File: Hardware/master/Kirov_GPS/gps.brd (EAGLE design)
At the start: 100 x 80 mm, 7 parts

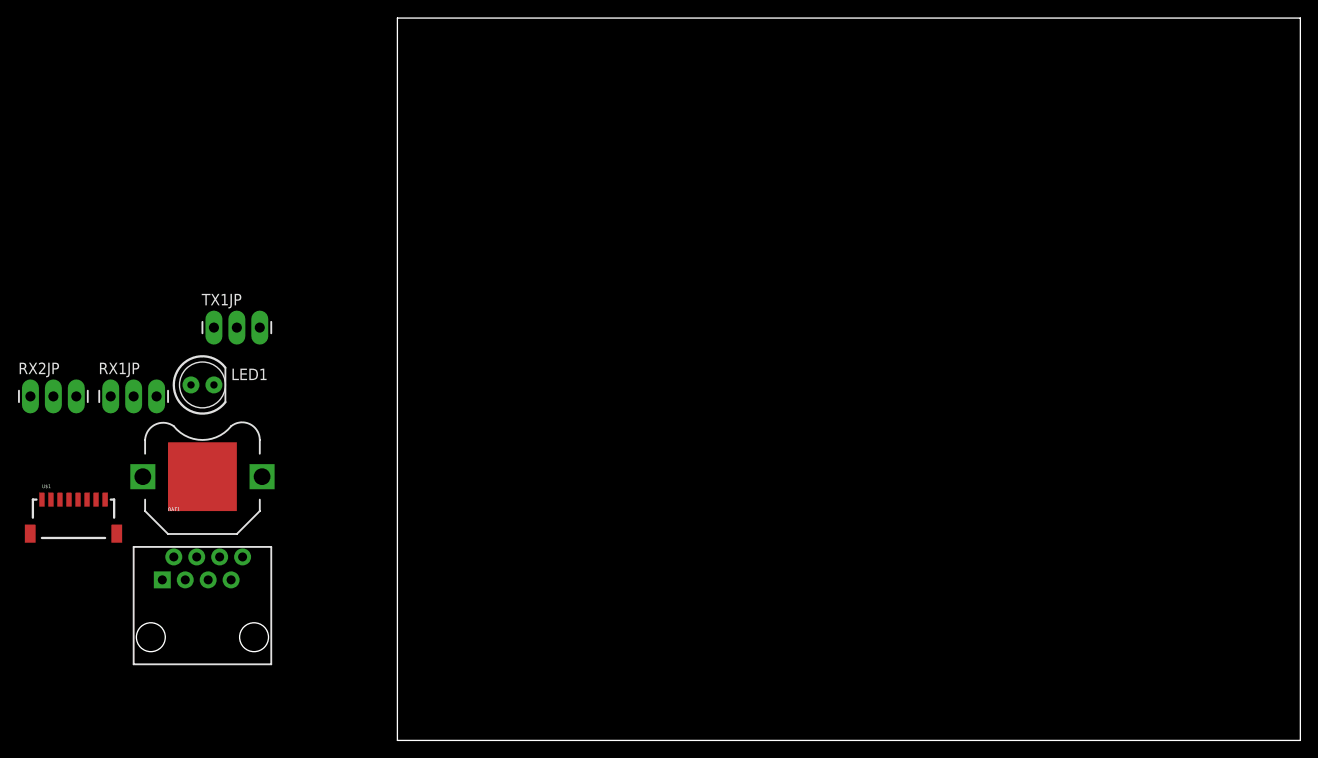
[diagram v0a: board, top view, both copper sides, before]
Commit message: added board layout and cap to schematic
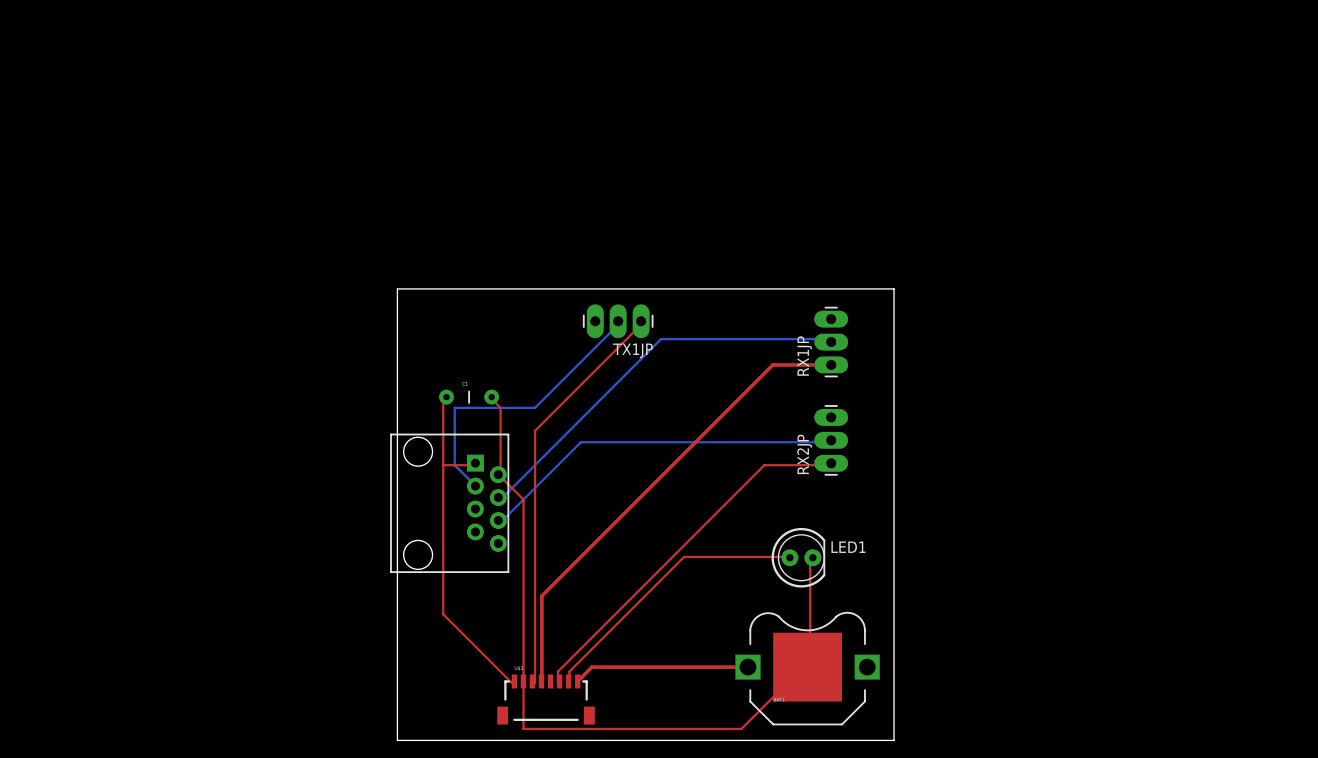
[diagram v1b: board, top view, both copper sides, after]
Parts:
- added C1: 100 uf, SparkFun-Passives:CAP-PTH-5MM
- moved RX2JP 89.0 mm to (48.0, 30.7), turned to 90 degrees
- moved RX1JP 79.9 mm to (48.0, 41.6), turned to 90 degrees
- moved BAT1 70.3 mm to (45.4, 8.12)
- moved LED1 69.0 mm to (44.7, 20.2)
- moved U$1 56.1 mm to (13.0, 6.53)
- moved TX1JP 47.3 mm to (27.0, 46.4), turned to 180 degrees
- moved GPS2ZYNQ 28.1 mm to (2.29, 26.3), turned to 270 degrees
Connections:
- net GND: now also C1.2
- net VCC: now also C1.1
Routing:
- net GND: track 0.00 -> 86.0 mm
- net RX1: track 0.00 -> 52.1 mm
- net TX1: track 0.00 -> 45.2 mm
- net ZRX1: track 0.00 -> 44.4 mm
- net RX2: track 0.00 -> 41.3 mm
- net ZRX2: track 0.00 -> 40.6 mm
- net VCC: track 0.00 -> 39.7 mm
- net ZTX1: track 0.00 -> 32.5 mm
- net PPS: track 0.00 -> 31.2 mm
- net BATT: track 0.00 -> 19.5 mm
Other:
- board size 100 x 80 mm -> 55 x 50 mm
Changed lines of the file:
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@@
 <setting verticaltext="up"/>
 </settings>
-<grid distance="0.05" unitdist="inch" unit="inch" style="lines" multiple="1" display="no" altdistance="0.025" altunitdist="inch" altunit="inch"/>
+<grid distance="1" unitdist="mm" unit="mm" style="lines" multiple="1" display="no" altdistance="0.1" altunitdist="mm" altunit="mm"/>
 <layers>
 <layer number="1" name="Top" color="4" fill="1" visible="yes" active="yes"/>
@@
 <board>
 <plain>
-<wire x1="0" y1="0" x2="100" y2="0" width="0" layer="20"/>
-<wire x1="100" y1="0" x2="100" y2="80" width="0" layer="20"/>
-<wire x1="100" y1="80" x2="0" y2="80" width="0" layer="20"/>
-<wire x1="0" y1="80" x2="0" y2="0" width="0" layer="20"/>
+<wire x1="0" y1="0" x2="55" y2="0" width="0" layer="20"/>
+<wire x1="55" y1="0" x2="55" y2="50" width="0" layer="20"/>
+<wire x1="55" y1="50" x2="0" y2="50" width="0" layer="20"/>
+<wire x1="0" y1="50" x2="0" y2="0" width="0" layer="20"/>
 </plain>
 <attributes>
@@
 </autorouter>
 <elements>
-<element name="U$1" library="SparkFun-Connectors" package="EB-85A" value="EB-85ASMD" x="-39.37" y="26.67"/>
-<element name="GPS2ZYNQ" library="SparkFun-Connectors" package="RJ45-8" value="RJ45-8PTH" x="-21.59" y="11.43"/>
-<element name="LED1" library="SparkFun-LED" package="LED5MM" value="" x="-21.59" y="39.37"/>
-<element name="BAT1" library="SparkFun-Electromechanical" package="BATTCON_12MM_PTH" value="" x="-21.59" y="29.21"/>
-<element name="TX1JP" library="SparkFun-Connectors" package="1X03_LONGPADS" value="" x="-20.32" y="45.72"/>
-<element name="RX1JP" library="SparkFun-Connectors" package="1X03_LONGPADS" value="" x="-31.75" y="38.1"/>
-<element name="RX2JP" library="SparkFun-Connectors" package="1X03_LONGPADS" value="" x="-40.64" y="38.1"/>
+<element name="U$1" library="SparkFun-Connectors" package="EB-85A" value="EB-85ASMD" x="12.96" y="6.53"/>
+<element name="GPS2ZYNQ" library="SparkFun-Connectors" package="RJ45-8" value="RJ45-8PTH" x="2.29" y="26.26" rot="R270"/>
+<element name="LED1" library="SparkFun-LED" package="LED5MM" value="" x="44.74" y="20.23"/>
+<element name="BAT1" library="SparkFun-Electromechanical" package="BATTCON_12MM_PTH" value="" x="45.43" y="8.12"/>
+<element name="TX1JP" library="SparkFun-Connectors" package="1X03_LONGPADS" value="" x="26.99" y="46.42" rot="R180"/>
+<element name="RX1JP" library="SparkFun-Connectors" package="1X03_LONGPADS" value="" x="48.04" y="41.58" rot="R90"/>
+<element name="RX2JP" library="SparkFun-Connectors" package="1X03_LONGPADS" value="" x="48.04" y="30.69" rot="R90"/>
+<element name="C1" library="SparkFun-Passives" package="CAP-PTH-5MM" value="100 uf" x="7.94" y="38.02"/>
 </elements>
 <signals>
@@
 <contactref element="U$1" pad="1"/>
 <contactref element="GPS2ZYNQ" pad="1"/>
-<wire x1="-26.035" y1="17.78" x2="-39.37" y2="26.67" width="0" layer="19" extent="1-1"/>
+<contactref element="C1" pad="1"/>
+<wire x1="5.08" y1="13.97" x2="12.7" y2="6.35" width="0.254" layer="1"/>
+<wire x1="5.08" y1="38.1" x2="5.08" y2="30.48" width="0.254" layer="1"/>
+<wire x1="5.08" y1="30.48" x2="5.08" y2="13.97" width="0.254" layer="1"/>
+<wire x1="12.7" y1="6.35" x2="12.96" y2="6.53" width="0.254" layer="1"/>
+<wire x1="5.08" y1="38.1" x2="5.44" y2="38.02" width="0.254" layer="1"/>
+<wire x1="5.08" y1="30.48" x2="8.89" y2="30.48" width="0.254" layer="1"/>
+<wire x1="8.89" y1="30.48" x2="8.64" y2="30.705" width="0.254" layer="1"/>
 </signal>
 <signal name="GND">
@@
 <contactref element="LED1" pad="K"/>
 <contactref element="GPS2ZYNQ" pad="2"/>
-<wire x1="-21.59" y1="29.21" x2="-20.32" y2="39.37" width="0" layer="19" extent="1-1"/>
-<wire x1="-24.765" y1="20.32" x2="-21.59" y2="29.21" width="0" layer="19" extent="1-1"/>
-<wire x1="-38.37" y1="26.67" x2="-24.765" y2="20.32" width="0" layer="19" extent="1-1"/>
+<contactref element="C1" pad="2"/>
+<wire x1="45.72" y1="8.89" x2="45.72" y2="20.32" width="0.254" layer="1"/>
+<wire x1="45.72" y1="20.32" x2="46.01" y2="20.23" width="0.254" layer="1"/>
+<wire x1="45.72" y1="8.89" x2="45.43" y2="8.12" width="0.254" layer="1"/>
+<wire x1="13.97" y1="26.67" x2="13.97" y2="6.35" width="0.254" layer="1"/>
+<wire x1="11.43" y1="29.21" x2="13.97" y2="26.67" width="0.254" layer="1"/>
+<wire x1="11.43" y1="36.83" x2="10.16" y2="38.1" width="0.254" layer="1"/>
+<wire x1="11.43" y1="29.21" x2="11.43" y2="36.83" width="0.254" layer="1"/>
+<wire x1="10.16" y1="38.1" x2="10.44" y2="38.02" width="0.254" layer="1"/>
+<wire x1="11.43" y1="29.21" x2="11.18" y2="29.435" width="0.254" layer="1"/>
+<wire x1="38.1" y1="1.27" x2="44.45" y2="7.62" width="0.254" layer="1"/>
+<wire x1="13.97" y1="1.27" x2="38.1" y2="1.27" width="0.254" layer="1"/>
+<wire x1="13.97" y1="6.35" x2="13.97" y2="1.27" width="0.254" layer="1"/>
+<wire x1="44.45" y1="7.62" x2="45.43" y2="8.12" width="0.254" layer="1"/>
+<wire x1="13.97" y1="6.35" x2="13.96" y2="6.53" width="0.254" layer="1"/>
 </signal>
 <signal name="TX1">
 <contactref element="U$1" pad="3"/>
 <contactref element="TX1JP" pad="1"/>
-<wire x1="-37.37" y1="26.67" x2="-20.32" y2="45.72" width="0" layer="19" extent="1-1"/>
+<wire x1="15.24" y1="34.29" x2="15.24" y2="6.35" width="0.254" layer="1"/>
+<wire x1="26.67" y1="45.72" x2="15.24" y2="34.29" width="0.254" layer="1"/>
+<wire x1="15.24" y1="6.35" x2="14.96" y2="6.53" width="0.254" layer="1"/>
+<wire x1="26.67" y1="45.72" x2="26.99" y2="46.42" width="0.254" layer="1"/>
 </signal>
 <signal name="RX1">
 <contactref element="U$1" pad="4"/>
 <contactref element="RX1JP" pad="1"/>
-<wire x1="-31.75" y1="38.1" x2="-36.37" y2="26.67" width="0" layer="19" extent="1-1"/>
+<wire x1="48.04" y1="41.58" x2="41.58" y2="41.58" width="0.4064" layer="1"/>
+<wire x1="41.58" y1="41.58" x2="16" y2="16" width="0.4064" layer="1"/>
+<wire x1="16" y1="16" x2="16" y2="6.57" width="0.4064" layer="1"/>
+<wire x1="16" y1="6.57" x2="15.96" y2="6.53" width="0.4064" layer="1"/>
 </signal>
 <signal name="TX2">
@@
 <contactref element="U$1" pad="6"/>
 <contactref element="RX2JP" pad="1"/>
-<wire x1="-40.64" y1="38.1" x2="-34.37" y2="26.67" width="0" layer="19" extent="1-1"/>
+<wire x1="17.78" y1="7.62" x2="17.78" y2="6.35" width="0.254" layer="1"/>
+<wire x1="40.64" y1="30.48" x2="17.78" y2="7.62" width="0.254" layer="1"/>
+<wire x1="46.99" y1="30.48" x2="40.64" y2="30.48" width="0.254" layer="1"/>
+<wire x1="17.78" y1="6.35" x2="17.96" y2="6.53" width="0.254" layer="1"/>
+<wire x1="46.99" y1="30.48" x2="48.04" y2="30.69" width="0.254" layer="1"/>
 </signal>
 <signal name="BATT">
 <contactref element="U$1" pad="8"/>
 <contactref element="BAT1" pad="VCC@1"/>
-<wire x1="-28.194" y1="29.21" x2="-32.37" y2="26.67" width="0" layer="19" extent="1-1"/>
+<wire x1="38.826" y1="8.12" x2="21.55" y2="8.12" width="0.4064" layer="1"/>
+<wire x1="21.55" y1="8.12" x2="19.96" y2="6.53" width="0.4064" layer="1"/>
 </signal>
 <signal name="PPS">
 <contactref element="U$1" pad="7"/>
 <contactref element="LED1" pad="A"/>
-<wire x1="-33.37" y1="26.67" x2="-22.86" y2="39.37" width="0" layer="19" extent="1-1"/>
+<wire x1="19.05" y1="7.62" x2="19.05" y2="6.35" width="0.254" layer="1"/>
+<wire x1="31.75" y1="20.32" x2="19.05" y2="7.62" width="0.254" layer="1"/>
+<wire x1="43.18" y1="20.32" x2="31.75" y2="20.32" width="0.254" layer="1"/>
+<wire x1="19.05" y1="6.35" x2="18.96" y2="6.53" width="0.254" layer="1"/>
+<wire x1="43.18" y1="20.32" x2="43.47" y2="20.23" width="0.254" layer="1"/>
 </signal>
 <signal name="ZTX1">
 <contactref element="GPS2ZYNQ" pad="3"/>
 <contactref element="TX1JP" pad="2"/>
-<wire x1="-23.495" y1="17.78" x2="-17.78" y2="45.72" width="0" layer="19" extent="1-1"/>
+<wire x1="6.35" y1="30.48" x2="8.89" y2="27.94" width="0.254" layer="16"/>
+<wire x1="6.35" y1="36.83" x2="6.35" y2="30.48" width="0.254" layer="16"/>
+<wire x1="15.24" y1="36.83" x2="6.35" y2="36.83" width="0.254" layer="16"/>
+<wire x1="24.13" y1="45.72" x2="15.24" y2="36.83" width="0.254" layer="16"/>
+<wire x1="8.89" y1="27.94" x2="8.64" y2="28.165" width="0.254" layer="16"/>
+<wire x1="24.13" y1="45.72" x2="24.45" y2="46.42" width="0.254" layer="16"/>
 </signal>
 <signal name="ZRX1">
 <contactref element="GPS2ZYNQ" pad="4"/>
 <contactref element="RX1JP" pad="2"/>
-<wire x1="-22.225" y1="20.32" x2="-29.21" y2="38.1" width="0" layer="19" extent="1-1"/>
+<wire x1="29.21" y1="44.45" x2="11.43" y2="26.67" width="0.254" layer="16"/>
+<wire x1="46.99" y1="44.45" x2="29.21" y2="44.45" width="0.254" layer="16"/>
+<wire x1="11.43" y1="26.67" x2="11.18" y2="26.895" width="0.254" layer="16"/>
+<wire x1="46.99" y1="44.45" x2="48.04" y2="44.12" width="0.254" layer="16"/>
 </signal>
 <signal name="ZRX2">
 <contactref element="GPS2ZYNQ" pad="6"/>
 <contactref element="RX2JP" pad="2"/>
-<wire x1="-38.1" y1="38.1" x2="-19.685" y2="20.32" width="0" layer="19" extent="1-1"/>
+<wire x1="20.32" y1="33.02" x2="11.43" y2="24.13" width="0.254" layer="16"/>
+<wire x1="46.99" y1="33.02" x2="20.32" y2="33.02" width="0.254" layer="16"/>
+<wire x1="11.43" y1="24.13" x2="11.18" y2="24.355" width="0.254" layer="16"/>
+<wire x1="46.99" y1="33.02" x2="48.04" y2="33.23" width="0.254" layer="16"/>
 </signal>
 </signals>
